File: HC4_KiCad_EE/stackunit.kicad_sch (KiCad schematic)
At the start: 12 parts, among them IC8 74HC377

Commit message: 振出しに戻る
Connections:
- net Level_A0: now also IC8.18 (D7); no longer IC8.13 (D4)
- net Level_A1: now also IC8.17 (D6); no longer IC8.14 (D5)
- net Level_A2: now also IC8.14 (D5); no longer IC8.17 (D6)
- net Level_A3: now also IC8.13 (D4); no longer IC8.18 (D7)

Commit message: 自動配線前最終チェック
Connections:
- net at RN8.5 (R4.2): now also LD22.1 (K); no longer LD19.1 (K)
- net at LD20.1 (K): now also RN8.7 (R2.2); no longer RN8.6 (R3.2)
- net at RN8.8 (R1.2): now also LD19.1 (K); no longer LD22.1 (K)
- net at RN7.5 (R4.2): now also LD15.1 (K); no longer LD18.1 (K)
- net at LD21.1 (K): now also RN8.6 (R3.2); no longer RN8.7 (R2.2)
- net at RN7.7 (R2.2): now also LD17.1 (K); no longer LD16.1 (K)
- net at RN7.6 (R3.2): now also LD16.1 (K); no longer LD17.1 (K)
- net at RN7.8 (R1.2): now also LD18.1 (K); no longer LD15.1 (K)
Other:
- moved on the sheet: RN7A, RN7B, RN7C, RN7D, RN8A, RN8B, RN8C, RN8D

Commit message: たぶん完成！！！！！！！
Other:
- title: HC4_CPU -> HC4e_CPU
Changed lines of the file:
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@@
 	(paper "A4")
 	(title_block
-		(title "HC4_CPU")
-		(date "2025-06-16")
+		(title "HC4e_CPU")
+		(date "2025-07-21")
 		(rev "1.0")
 	)

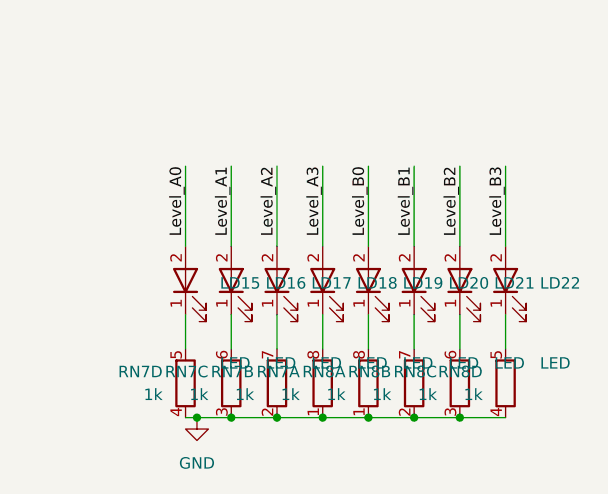
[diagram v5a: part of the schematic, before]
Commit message: feat:HC4e改版,BOMを令和最新版に更新,KiCadを10に更新
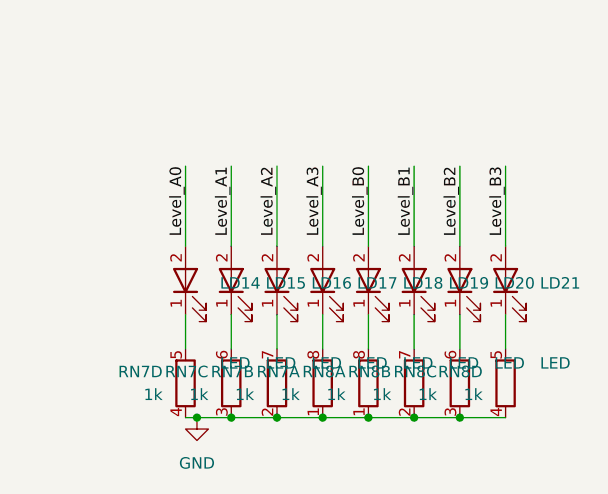
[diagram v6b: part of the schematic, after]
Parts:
- renumbered LD15 to LD14, LD16 to LD15, LD17 to LD16, LD18 to LD17, LD19 to LD18, LD20 to LD19, LD21 to LD20, LD22 to LD21

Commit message: 基板を若干改版、フットプリントの指定が外れていたのを修正
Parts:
- CP8: LCSC PN (none) -> C14663
- RN7, RN8: LCSC PN (none) -> C20197
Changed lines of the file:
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@@
+			)
+		)
+		(property "LCSC PN" "C20197"
+			(at 190.5 154.94 0)
+			(hide yes)
+			(show_name no)
+			(do_not_autoplace no)
+			(effects
+				(font
+					(size 1.27 1.27)
+				)
 			)
 		)
@@
 			)
 		)
+		(property "LCSC PN" ""
+			(at 180.34 143.51 90)
+			(hide yes)
+			(show_name no)
+			(do_not_autoplace no)
+			(effects
+				(font
+					(size 1.27 1.27)
+				)
+			)
+		)
 		(pin "1"
 		)
@@
 			)
 		)
+		(property "LCSC PN" ""
+			(at 190.5 143.51 90)
+			(hide yes)
+			(show_name no)
+			(do_not_autoplace no)
+			(effects
+				(font
+					(size 1.27 1.27)
+				)
+			)
+		)
 		(pin "1"
 		)
@@
 		)
 		(property "Description" "8-bit Register"
+			(at 58.42 95.25 0)
+			(hide yes)
+			(show_name no)
+			(do_not_autoplace no)
+			(effects
+				(font
+					(size 1.27 1.27)
+				)
+			)
+		)
+		(property "LCSC PN" ""
 			(at 58.42 95.25 0)
 			(hide yes)
@@
 			)
 		)
+		(property "LCSC PN" "C20197"
+			(at 154.94 154.94 0)
+			(hide yes)
+			(show_name no)
+			(do_not_autoplace no)
+			(effects
+				(font
+					(size 1.27 1.27)
+				)
+			)
+		)
 		(pin "5"
 		)
@@
 			)
 		)
+		(property "LCSC PN" ""
+			(at 170.18 143.51 90)
+			(hide yes)
+			(show_name no)
+			(do_not_autoplace no)
+			(effects
+				(font
+					(size 1.27 1.27)
+				)
+			)
+		)
 		(pin "1"
 		)
@@
 		(property "Description" "Light emitting diode"
 			(at 175.26 143.51 0)
+			(hide yes)
+			(show_name no)
+			(do_not_autoplace no)
+			(effects
+				(font
+					(size 1.27 1.27)
+				)
+			)
+		)
+		(property "LCSC PN" ""
+			(at 175.26 143.51 90)
 			(hide yes)
 			(show_name no)
@@
 			)
 		)
+		(property "LCSC PN" "C20197"
+			(at 175.26 154.94 0)
+			(hide yes)
+			(show_name no)
+			(do_not_autoplace no)
+			(effects
+				(font
+					(size 1.27 1.27)
+				)
+			)
+		)
 		(pin "3"
 		)
@@
 			)
 		)
+		(property "LCSC PN" "C20197"
+			(at 180.34 154.94 0)
+			(hide yes)
+			(show_name no)
+			(do_not_autoplace no)
+			(effects
+				(font
+					(size 1.27 1.27)
+				)
+			)
+		)
 		(pin "3"
 		)
@@
 			)
 		)
+		(property "LCSC PN" "C20197"
+			(at 165.1 154.94 0)
+			(hide yes)
+			(show_name no)
+			(do_not_autoplace no)
+			(effects
+				(font
+					(size 1.27 1.27)
+				)
+			)
+		)
 		(pin "5"
 		)
@@
 			)
 		)
+		(property "LCSC PN" ""
+			(at 165.1 143.51 90)
+			(hide yes)
+			(show_name no)
+			(do_not_autoplace no)
+			(effects
+				(font
+					(size 1.27 1.27)
+				)
+			)
+		)
 		(pin "1"
 		)
@@
 			)
 		)
+		(property "LCSC PN" "C14663"
+			(at 100.33 149.86 0)
+			(hide yes)
+			(show_name no)
+			(do_not_autoplace no)
+			(effects
+				(font
+					(size 1.27 1.27)
+				)
+			)
+		)
 		(pin "1"
 		)
@@
 		(property "Description" "Light emitting diode"
 			(at 154.94 143.51 0)
+			(hide yes)
+			(show_name no)
+			(do_not_autoplace no)
+			(effects
+				(font
+					(size 1.27 1.27)
+				)
+			)
+		)
+		(property "LCSC PN" ""
+			(at 154.94 143.51 90)
 			(hide yes)
 			(show_name no)
@@
 			)
 		)
+		(property "LCSC PN" "C20197"
+			(at 185.42 154.94 0)
+			(hide yes)
+			(show_name no)
+			(do_not_autoplace no)
+			(effects
+				(font
+					(size 1.27 1.27)
+				)
+			)
+		)
 		(pin "3"
 		)
@@
 			)
 		)
+		(property "LCSC PN" "C20197"
+			(at 160.02 154.94 0)
+			(hide yes)
+			(show_name no)
+			(do_not_autoplace no)
+			(effects
+				(font
+					(size 1.27 1.27)
+				)
+			)
+		)
 		(pin "5"
 		)
@@
 			)
 		)
+		(property "LCSC PN" ""
+			(at 185.42 143.51 90)
+			(hide yes)
+			(show_name no)
+			(do_not_autoplace no)
+			(effects
+				(font
+					(size 1.27 1.27)
+				)
+			)
+		)
 		(pin "1"
 		)
@@
 		(property "Description" "Light emitting diode"
 			(at 160.02 143.51 0)
+			(hide yes)
+			(show_name no)
+			(do_not_autoplace no)
+			(effects
+				(font
+					(size 1.27 1.27)
+				)
+			)
+		)
+		(property "LCSC PN" ""
+			(at 160.02 143.51 90)
 			(hide yes)
 			(show_name no)
@@
 			(at 170.18 154.94 0)
 			(hide yes)
+			(show_name no)
+			(do_not_autoplace no)
+			(effects
+				(font
+					(size 1.27 1.27)
+				)
+			)
+		)
+		(property "LCSC PN" "C20197"
+			(at 170.18 154.94 0)
+			(hide yes)

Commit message: HC4eRev2完成
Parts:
- IC8: footprint Package_SO:TSSOP-20_4.4x6.5mm_P0.65mm -> Package_SO:SOIC-20W_7.5x12.8mm_P1.27mm
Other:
- company: (none) -> Dengiken
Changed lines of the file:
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@@
 	(title_block
 		(title "HC4e_CPU")
-		(date "2026-03-19")
+		(date "2026-05-23")
 		(rev "2.0")
+		(company "Dengiken")
 	)
 	(junction
@@
 			)
 		)
-		(property "Footprint" "Package_SO:TSSOP-20_4.4x6.5mm_P0.65mm"
+		(property "Footprint" "Package_SO:SOIC-20W_7.5x12.8mm_P1.27mm"
 			(at 58.42 95.25 0)
 			(hide yes)
